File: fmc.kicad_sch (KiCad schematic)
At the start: 22 parts, among them P1 ASP-134488-01, Q1 FDN335N, Q2 FDN335N

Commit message: Completed Schematic
Completed Schematic Draft
- Includes careful pin mapping to avoid conflicts with other firmwares
- Roughed out LCB layout high speed traces, and FMC breakouts.

Layout and BOM are still WIP
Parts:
- P1: symbol rf-input-fmc:ASP-134488-01 -> evr-fmc:ASP-134488-01
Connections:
- net D_Output0: now also P1.G12
- net D_Output1: now also P1.G13
- net D_Output10: now also P1.C18
- net D_Output11: now also P1.C19
- net D_Output12: now also P1.G18
- net D_Output13: now also P1.G19
- net D_Output14: now also P1.G21
- net D_Output15: now also P1.G22
- net D_Output2: now also P1.D14
- net D_Output3: now also P1.D15
- net D_Output4: now also P1.C14
- net D_Output5: now also P1.C15
- net D_Output6: now also P1.G15
- net D_Output7: now also P1.G16
- net D_Output8: now also P1.D17
- net D_Output9: now also P1.D18
- net Cleaner_SPI_0.DIN: now reaches P1.G10
- net Cleaner_SPI_1.OE: now reaches P1.G24
- net Cleaner_SPI_1.DIN: now reaches P1.G25
- net Cleaned_CLK_0.P: now reaches P1.G6
- net Cleaned_CLK_0.N: now reaches P1.G7
- net Cleaner_SPI_0.OE: now reaches P1.G9
- net Cleaner_Fault_0.LOL: now reaches P1.H10
- net Cleaner_SPI_0.DOUT: now reaches P1.H11
- net Cleaner_Fault_1.INTR: now reaches P1.H25
- net Cleaner_Fault_1.LOS_XO: now reaches P1.H26
- net Cleaner_Fault_1.LOL: now reaches P1.H28
- net Cleaner_SPI_1.DOUT: now reaches P1.H29
- net Cleaner_Fault_0.INTR: now reaches P1.H7
- net Cleaner_Fault_0.LOS_XO: now reaches P1.H8
- net Cleaner_SPI_0.CLK: now reaches P1.D12
- net Cleaned_CLK_1.P: now reaches P1.D20
- net Cleaned_CLK_1.N: now reaches P1.D21
- net Cleaner_SPI_1.CLK: now reaches P1.D24
- net Cleaner_SPI_1.CS: now reaches P1.D26
- net Cleaner_~{RST}_1: now reaches P1.D27
- net Recovered_CLK_0.N: now reaches P1.D8
- net Recovered_CLK_0.P: now reaches P1.D9
- net Cleaner_SPI_0.CS: now reaches P1.C10
- net Cleaner_~{RST}_0: now reaches P1.C11
- net Recovered_CLK_1.N: now reaches P1.C22
- net Recovered_CLK_1.P: now reaches P1.C23
- net FMC_CLK0_M2C.N: no longer names the net of P1.H5
- net FMC_CLK0_M2C.P: no longer names the net of P1.H4
- net FMC_CLK1_M2C.N: no longer names the net of P1.G3
- net FMC_CLK1_M2C.P: no longer names the net of P1.G2
- net P1_12P0V renamed +12V_FMC
- no-connect marks 214 -> 177
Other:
- note added: "FMC_LA_0_N_CC"
- note added: "FMC_LA_0_P_CC"
- note added: "FMC_LA_17_N_CC"
- note added: "FMC_LA_17_P_CC"
- note added: "FMC_LA_18_N_CC"
- note added: "FMC_LA_18_P_CC"
- note added: "FMC_LA_1_N_CC"
- note added: "FMC_LA_1_P_CC"
- note removed: "FMC_LA_0_N"
- note removed: "FMC_LA_0_P"
- note removed: "FMC_LA_17_N"
- note removed: "FMC_LA_17_P"
- note removed: "FMC_LA_18_N"
- note removed: "FMC_LA_18_P"
- note removed: "FMC_LA_1_N"
- note removed: "FMC_LA_1_P"
- moved on the sheet: P1A, P1B, P1C, P1D

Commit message: Updated Schematic and continued layout work
schematic:
- Added 0ohm resistor in power section
- Added pull up and down to digital lines to define powerup behavior
- Added some power filter between jitter cleaner IC's

layout:
-Overall Still WIP
-defined all needed fmc pins
-started layout of critical clock signals and connector locations.
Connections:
- net Cleaner_SPI_0.DIN renamed Cleaner_SPI_0.SDI
- net Cleaner_SPI_0.DOUT renamed Cleaner_SPI_0.SDO
- net Cleaner_SPI_1.DIN renamed Cleaner_SPI_1.SDI
- net Cleaner_SPI_1.DOUT renamed Cleaner_SPI_1.SDO
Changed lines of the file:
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@@
 		)
 	)
-	(label "Cleaner_SPI_0.DIN"
+	(label "Cleaner_SPI_0.SDI"
 		(at 300.99 49.53 0)
 		(effects
@@
 		)
 	)
-	(label "Cleaner_SPI_0.DOUT"
+	(label "Cleaner_SPI_0.SDO"
 		(at 360.68 52.07 0)
 		(effects
@@
 		)
 	)
-	(label "Cleaner_SPI_0.DIN"
+	(label "Cleaner_SPI_0.SDI"
 		(at 86.36 45.72 180)
 		(effects
@@
 		)
 	)
-	(label "Cleaner_SPI_1.DIN"
+	(label "Cleaner_SPI_1.SDI"
 		(at 86.36 99.06 180)
 		(effects
@@
 		)
 	)
-	(label "Cleaner_SPI_0.DOUT"
+	(label "Cleaner_SPI_0.SDO"
 		(at 86.36 48.26 180)
 		(effects
@@
 		)
 	)
-	(label "Cleaner_SPI_1.DIN"
+	(label "Cleaner_SPI_1.SDI"
 		(at 300.99 87.63 0)
 		(effects
@@
 		)
 	)
-	(label "Cleaner_SPI_1.DOUT"
+	(label "Cleaner_SPI_1.SDO"
 		(at 86.36 101.6 180)
 		(effects
@@
 		)
 	)
-	(label "Cleaner_SPI_1.DOUT"
+	(label "Cleaner_SPI_1.SDO"
 		(at 360.68 97.79 0)
 		(effects
@@
 			(at 30.48 201.93 0)
 			(effects
-				(font
-					(size 1.27 1.27)
-				)
-				(hide yes)
-			)
-		)
-		(property "Sim.Enable" "0"
-			(at 30.48 201.93 0)
-			(effects

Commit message: Schematic Updates
-Added Heartbeat LED
-Assigned Jitter cleaner OE to FPGA pins
-Changed LDO parts
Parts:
- added D4: LED_Green, LED_SMD:LED_0603_1608Metric, symbol Device:LED
- added Q3: FDN335N, Package_TO_SOT_SMD:SOT-23, symbol Transistor_FET:Q_NMOS_GSD
- added R95: 1k, Resistor_SMD:R_0603_1608Metric, symbol Device:R_Small_US
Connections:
- net GND: now also Q3.2 (S)
- net VDD3P3V: now also R95.2
- net Cleaner_~{OE}_1: now reaches P1.H22
- net Cleaner_~{OE}_0: now reaches P1.C26
- net Heartbeat_LED: now reaches P1.C27
- net Heartbeat_LED: now also Q3.1 (G)
- new net: D4.2 (A), R95.1
- new net: D4.1 (K), Q3.3 (D)
- no-connect marks 177 -> 174
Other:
- moved on the sheet: D1, D2, D3, P1G, P1H, P1I, P1J, Q1, Q2, R18, R19, R20

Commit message: Layout draft nearly complete
- Changed some digital IO pinout on the FMC
- Most areas routed
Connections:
- net Cleaner_SPI_0.CLK: now also P1.C10; no longer P1.D12
- net Cleaner_SPI_0.CS: now also P1.G10; no longer P1.C10
- net Cleaner_SPI_0.OE: now also P1.D12; no longer P1.G9
- net Cleaner_SPI_0.SDI: now also P1.C11; no longer P1.G10
- net Cleaner_SPI_1.CS: now also P1.G25; no longer P1.D26
- net Cleaner_SPI_1.OE: now also P1.D27; no longer P1.G24
- net Cleaner_SPI_1.SDI: now also P1.D26; no longer P1.G25
- net Cleaner_~{RST}_0: now also P1.G9; no longer P1.C11
- net Cleaner_~{RST}_1: now also P1.G24; no longer P1.D27
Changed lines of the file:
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@@
+		)
+	)
+	(label "Cleaner_SPI_1.SDI"
+		(at 227.33 88.9 0)
+		(effects
+			(font
+				(size 1.27 1.27)
+			)
+			(justify left bottom)
 		)
 	)
@@
 		)
 	)
-	(label "Cleaner_SPI_0.SDI"
-		(at 300.99 49.53 0)
-		(effects
-			(font
-				(size 1.27 1.27)
-			)
-			(justify left bottom)
-		)
-	)
 	(label "Cleaned_CLK_1.P"
 		(at 227.33 73.66 0)
@@
 		)
 	)
+	(label "Cleaner_SPI_1.CLK"
+		(at 227.33 83.82 0)
+		(effects
+			(font
+				(size 1.27 1.27)
+			)
+			(justify left bottom)
+		)
+	)
 	(label "Cleaner_Fault_0.LOL"
 		(at 86.36 69.85 180)
@@
 		)
 	)
-	(label "Cleaner_~{RST}_1"
-		(at 227.33 91.44 0)
-		(effects
-			(font
-				(size 1.27 1.27)
-			)
-			(justify left bottom)
-		)
-	)
 	(label "Cleaner_Fault_1.INTR"
 		(at 360.68 87.63 0)
@@
 		)
 	)
+	(label "Cleaner_SPI_1.CS"
+		(at 300.99 87.63 0)
+		(effects
+			(font
+				(size 1.27 1.27)
+			)
+			(justify left bottom)
+		)
+	)
 	(label "D_Output6"
 		(at 300.99 62.23 0)
@@
 		)
 	)
+	(label "Cleaner_SPI_1.OE"
+		(at 227.33 91.44 0)
+		(effects
+			(font
+				(size 1.27 1.27)
+			)
+			(justify left bottom)
+		)
+	)
 	(label "EEPROM_SCL"
 		(at 160.02 99.06 0)
@@
 		)
 	)
-	(label "Cleaner_SPI_0.CLK"
-		(at 227.33 53.34 0)
-		(effects
-			(font
-				(size 1.27 1.27)
-			)
-			(justify left bottom)
-		)
-	)
 	(label "EEPROM_GA1"
 		(at 146.05 67.31 180)
@@
 		)
 	)
-	(label "Cleaner_SPI_1.CS"
-		(at 227.33 88.9 0)
-		(effects
-			(font
-				(size 1.27 1.27)
-			)
-			(justify left bottom)
-		)
-	)
 	(label "Cleaned_CLK_0.P"
 		(at 300.99 39.37 0)
@@
 		)
 	)
-	(label "Cleaner_SPI_0.OE"
-		(at 300.99 46.99 0)
+	(label "Cleaner_SPI_0.CS"
+		(at 300.99 49.53 0)
 		(effects
 			(font
@@
 		)
 	)
+	(label "Cleaner_~{RST}_0"
+		(at 300.99 46.99 0)
+		(effects
+			(font
+				(size 1.27 1.27)
+			)
+			(justify left bottom)
+		)
+	)
 	(label "D_Output7"
 		(at 300.99 64.77 0)
@@
 		)
 	)
-	(label "Cleaner_SPI_1.SDI"
-		(at 300.99 87.63 0)
-		(effects
-			(font
-				(size 1.27 1.27)
-			)
-			(justify left bottom)
-		)
-	)
 	(label "D_Output1"
 		(at 146.05 20.32 180)
@@
 		)
 	)
-	(label "Cleaner_~{RST}_0"
-		(at 156.21 50.8 0)
-		(effects
-			(font
-				(size 1.27 1.27)
-			)
-			(justify left bottom)
-		)
-	)
-	(label "Cleaner_SPI_0.CS"
-		(at 156.21 48.26 0)
-		(effects
-			(font
-				(size 1.27 1.27)
-			)
-			(justify left bottom)
-		)
-	)
 	(label "EEPROM_GA0"
 		(at 146.05 64.77 180)
@@
 		)
 	)
+	(label "Cleaner_SPI_0.CLK"
+		(at 156.21 48.26 0)
+		(effects
+			(font
+				(size 1.27 1.27)
+			)
+			(justify left bottom)
+		)
+	)
 	(label "Cleaner_~{OE}_1"
 		(at 360.68 80.01 0)
@@
 		)
 	)
+	(label "Cleaner_SPI_0.OE"
+		(at 227.33 53.34 0)
+		(effects
+			(font
+				(size 1.27 1.27)
+			)
+			(justify left bottom)
+		)
+	)
 	(label "FMC_GBTCLK1.P"
 		(at 140.97 190.5 0)
@@
 		)
 	)
-	(label "Cleaner_SPI_1.OE"
+	(label "Cleaner_~{RST}_1"
 		(at 300.99 85.09 0)
 		(effects
@@
 		)
 	)
-	(label "Cleaner_SPI_1.CLK"
-		(at 227.33 83.82 0)
-		(effects
-			(font
-				(size 1.27 1.27)
-			)
-			(justify left bottom)
-		)
-	)
 	(label "Cleaner_SPI_0.CLK"
 		(at 86.36 43.18 180)
@@
 		(effects
 			(font
+				(size 1.27 1.27)
+			)
+			(justify left bottom)
+		)
+	)
+	(label "Cleaner_SPI_0.SDI"
+		(at 156.21 50.8 0)
+		(effects
+			(font

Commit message: Draft Layout Complete
-Draft Layout Complete
- Silkscreen need to be complete
- some Digital IO swapped FMC pins
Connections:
- net D_Output10: now also P1.D17; no longer P1.C18
- net D_Output11: now also P1.D18; no longer P1.C19
- net D_Output12: now also P1.G21; no longer P1.G18
- net D_Output13: now also P1.G22; no longer P1.G19
- net D_Output14: now also P1.C18; no longer P1.G21
- net D_Output15: now also P1.C19; no longer P1.G22
- net D_Output4: now also P1.G15; no longer P1.C14
- net D_Output5: now also P1.G16; no longer P1.C15
- net D_Output6: now also P1.C14; no longer P1.G15
- net D_Output7: now also P1.C15; no longer P1.G16
- net D_Output8: now also P1.G18; no longer P1.D17
- net D_Output9: now also P1.G19; no longer P1.D18
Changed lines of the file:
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@@
 	)
 	(label "D_Output12"
-		(at 300.99 69.85 0)
+		(at 300.99 77.47 0)
 		(effects
 			(font
@@
 	)
 	(label "D_Output4"
-		(at 156.21 58.42 0)
+		(at 300.99 62.23 0)
 		(effects
 			(font
@@
 	)
 	(label "D_Output11"
-		(at 156.21 71.12 0)
+		(at 227.33 68.58 0)
 		(effects
 			(font
@@
 		)
 	)
-	(label "D_Output6"
-		(at 300.99 62.23 0)
-		(effects
-			(font
-				(size 1.27 1.27)
-			)
-			(justify left bottom)
-		)
-	)
 	(label "Cleaner_~{OE}_0"
 		(at 86.36 58.42 180)
@@
 	)
 	(label "D_Output14"
-		(at 300.99 77.47 0)
+		(at 156.21 68.58 0)
 		(effects
 			(font
@@
 	)
 	(label "D_Output9"
-		(at 227.33 68.58 0)
+		(at 300.99 72.39 0)
 		(effects
 			(font
@@
 	)
 	(label "D_Output5"
-		(at 156.21 60.96 0)
+		(at 300.99 64.77 0)
 		(effects
 			(font
@@
 	)
 	(label "D_Output8"
-		(at 227.33 66.04 0)
+		(at 300.99 69.85 0)
 		(effects
 			(font
@@
 	)
 	(label "D_Output15"
+		(at 156.21 71.12 0)
+		(effects
+			(font
+				(size 1.27 1.27)
+			)
+			(justify left bottom)
+		)
+	)
+	(label "D_Output13"
 		(at 300.99 80.01 0)
-		(effects
-			(font
-				(size 1.27 1.27)
-			)
-			(justify left bottom)
-		)
-	)
-	(label "D_Output13"
-		(at 300.99 72.39 0)
 		(effects
 			(font
@@
 		)
 	)
-	(label "D_Output7"
-		(at 300.99 64.77 0)
-		(effects
-			(font
-				(size 1.27 1.27)
-			)
-			(justify left bottom)
-		)
-	)
 	(label "Cleaner_Fault_0.INTR"
 		(at 86.36 64.77 180)
@@
 		)
 	)
+	(label "D_Output6"
+		(at 156.21 58.42 0)
+		(effects
+			(font
+				(size 1.27 1.27)
+			)
+			(justify left bottom)
+		)
+	)
 	(label "D_Output7"
 		(at 146.05 35.56 180)
@@
 	)
 	(label "D_Output10"
-		(at 156.21 68.58 0)
+		(at 227.33 66.04 0)
 		(effects
 			(font
@@
 		(effects
 			(font
+				(size 1.27 1.27)
+			)
+			(justify left bottom)
+		)
+	)
+	(label "D_Output7"
+		(at 156.21 60.96 0)
+		(effects
+			(font

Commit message: Final Draft - Ready to Review
Things to do:
Round diff traces before generting fabrication files
Change name of project to 'trigger output fmc'
Align this with recent updates to fmc-template

Updates:
- Cleaned up BOM
- Arranged silkscreen and fab layers
- Shortened power traces from LDOs to Jitter Cleaner IC
- Fixed traces/planes with sharp corners
- Straightened out all MMCX Test Ports
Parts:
- C34, C35: Manufacturer Murata Electronics -> Murata
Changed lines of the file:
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@@
 			)
 		)
-		(property "Manufacturer" "Murata Electronics"
+		(property "Manufacturer" "Murata"
 			(at 74.93 238.76 0)
 			(effects
@@
 			)
 		)
-		(property "Manufacturer" "Murata Electronics"
+		(property "Manufacturer" "Murata"
 			(at 39.37 237.49 0)
 			(effects

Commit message: Final Draft - Ready for review
Updates:
- Changed area behind FMC connector to match the new Osprey FMC template
  - This includes a new 12V LED, more robust power input traces, arranged elements for readability.

Things to do:
Round diff traces before generating fabrication files
Change name of project to 'trigger output fmc'
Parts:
- added C79: 22uF, Capacitor_SMD:C_0805_2012Metric, symbol Device:C_Small
- added D5: Green, LED_SMD:LED_0603_1608Metric, symbol Device:LED
- added R100: 8.2k, Resistor_SMD:R_0603_1608Metric, symbol Device:R_Small_US
- added R101, R102, R103: 100k, Resistor_SMD:R_0603_1608Metric, symbol Device:R_Small_US
- D1, D2, D3, D4: value LED_Green -> Green
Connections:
- net +12V_FMC: now also R100.2
- net GND: now also C79.2, D5.1 (K), R101.1, R102.1, R103.1
- net Heartbeat_LED: now also R103.2
- net P1_3P3VAUX renamed 3P3VAUX
- net P1_PG_C2M renamed PG_C2M
- net PG_C2M: now also R101.2
- net P1_PRSNT renamed PRSNT
- net P1_TDI renamed TDI
- net P1_TDO renamed TDO
- net P1_VADJ renamed VADJ
- net VADJ: now also C79.1, R102.2
- new net: D5.2 (A), R100.1
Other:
- title: FMC Template -> Trigger Output FMC
- moved on the sheet: C34, C35, D2, D3, D4, H1, H2, H3, H4, Q2, Q3, R19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

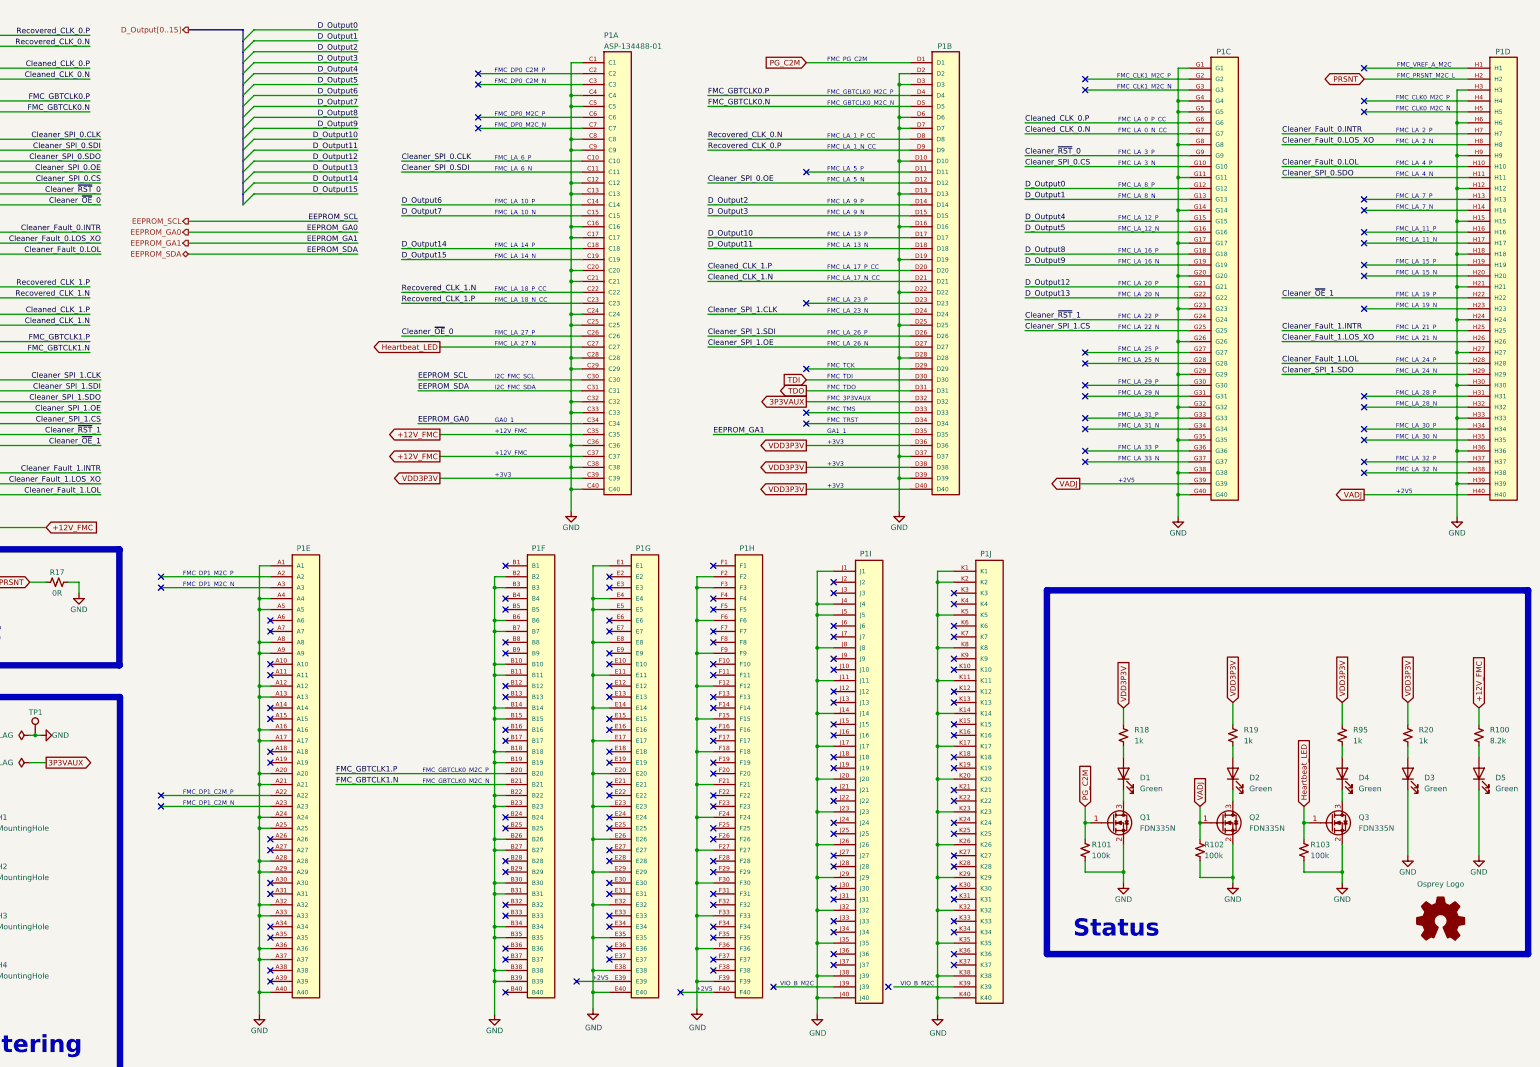
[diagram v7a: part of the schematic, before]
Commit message: Changed Trigger Outputs Topology
- Changed to a comp to digital TX design
- Added power section to support this change
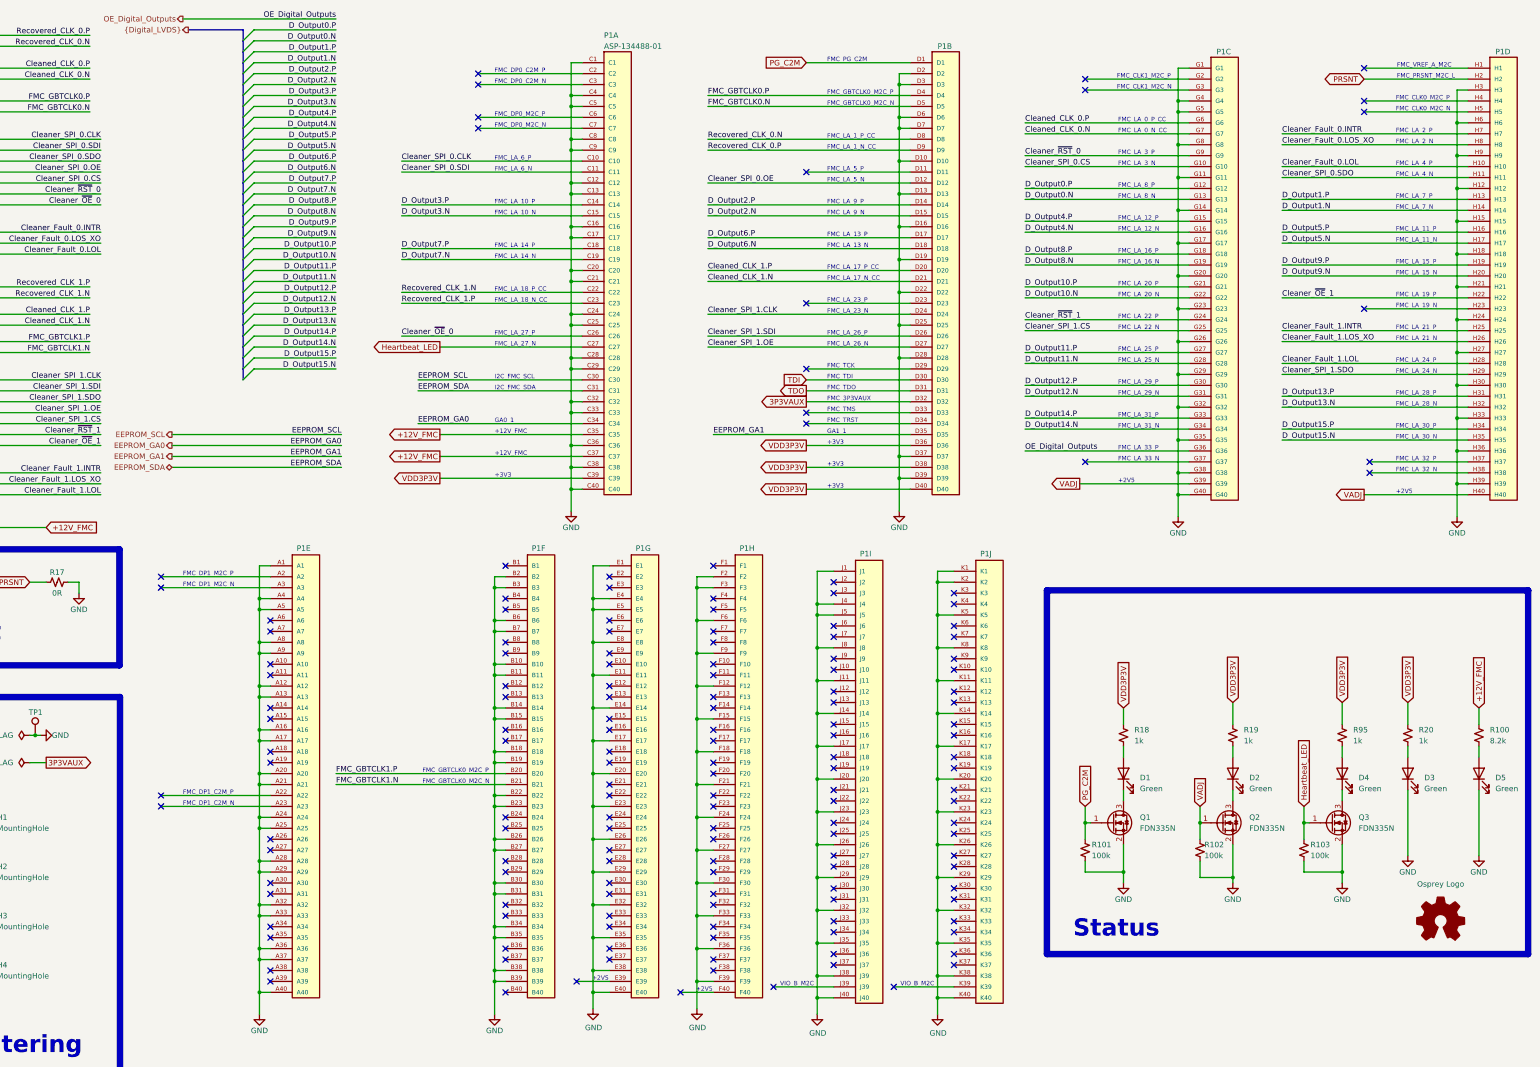
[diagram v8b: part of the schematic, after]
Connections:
- net D_Output11.P: now reaches P1.G27
- net D_Output11.N: now reaches P1.G28
- net D_Output12.P: now reaches P1.G30
- net D_Output12.N: now reaches P1.G31
- net D_Output14.P: now reaches P1.G33
- net D_Output14.N: now reaches P1.G34
- net OE_Digital_Outputs: now reaches P1.G36
- net D_Output1.P: now reaches P1.H13
- net D_Output1.N: now reaches P1.H14
- net D_Output5.P: now reaches P1.H16
- net D_Output5.N: now reaches P1.H17
- net D_Output9.P: now reaches P1.H19
- net D_Output9.N: now reaches P1.H20
- net D_Output13.P: now reaches P1.H31
- net D_Output13.N: now reaches P1.H32
- net D_Output15.P: now reaches P1.H34
- net D_Output15.N: now reaches P1.H35
- net D_Output0 renamed D_Output0.P
- net D_Output1 renamed D_Output0.N
- net D_Output10 renamed D_Output6.P
- net D_Output11 renamed D_Output6.N
- net D_Output12 renamed D_Output10.P
- net D_Output13 renamed D_Output10.N
- net D_Output14 renamed D_Output7.P
- net D_Output15 renamed D_Output7.N
- net D_Output2 renamed D_Output2.P
- net D_Output3 renamed D_Output2.N
- net D_Output4 renamed D_Output4.P
- net D_Output5 renamed D_Output4.N
- net D_Output6 renamed D_Output3.P
- net D_Output7 renamed D_Output3.N
- net D_Output8 renamed D_Output8.P
- net D_Output9 renamed D_Output8.N
- no-connect marks 174 -> 157
